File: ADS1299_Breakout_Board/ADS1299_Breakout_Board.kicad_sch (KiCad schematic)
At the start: 41 parts, among them J1 Conn_01x08_Pin, J2 Conn_01x08_Pin, J3 Conn_01x08_Pin, J4 Conn_01x08_Pin, J5 Conn_01x08_Pin, U1 TPD4E1B06DRLR, U2 ADS1299IPAG, U3 TPD4E1B06DRLR, U4 TPD4E1B06DRLR, U5 TPD4E1B06DRLR, U6 TPD4E1B06DRLR, U7 TPD4E1B06DRLR

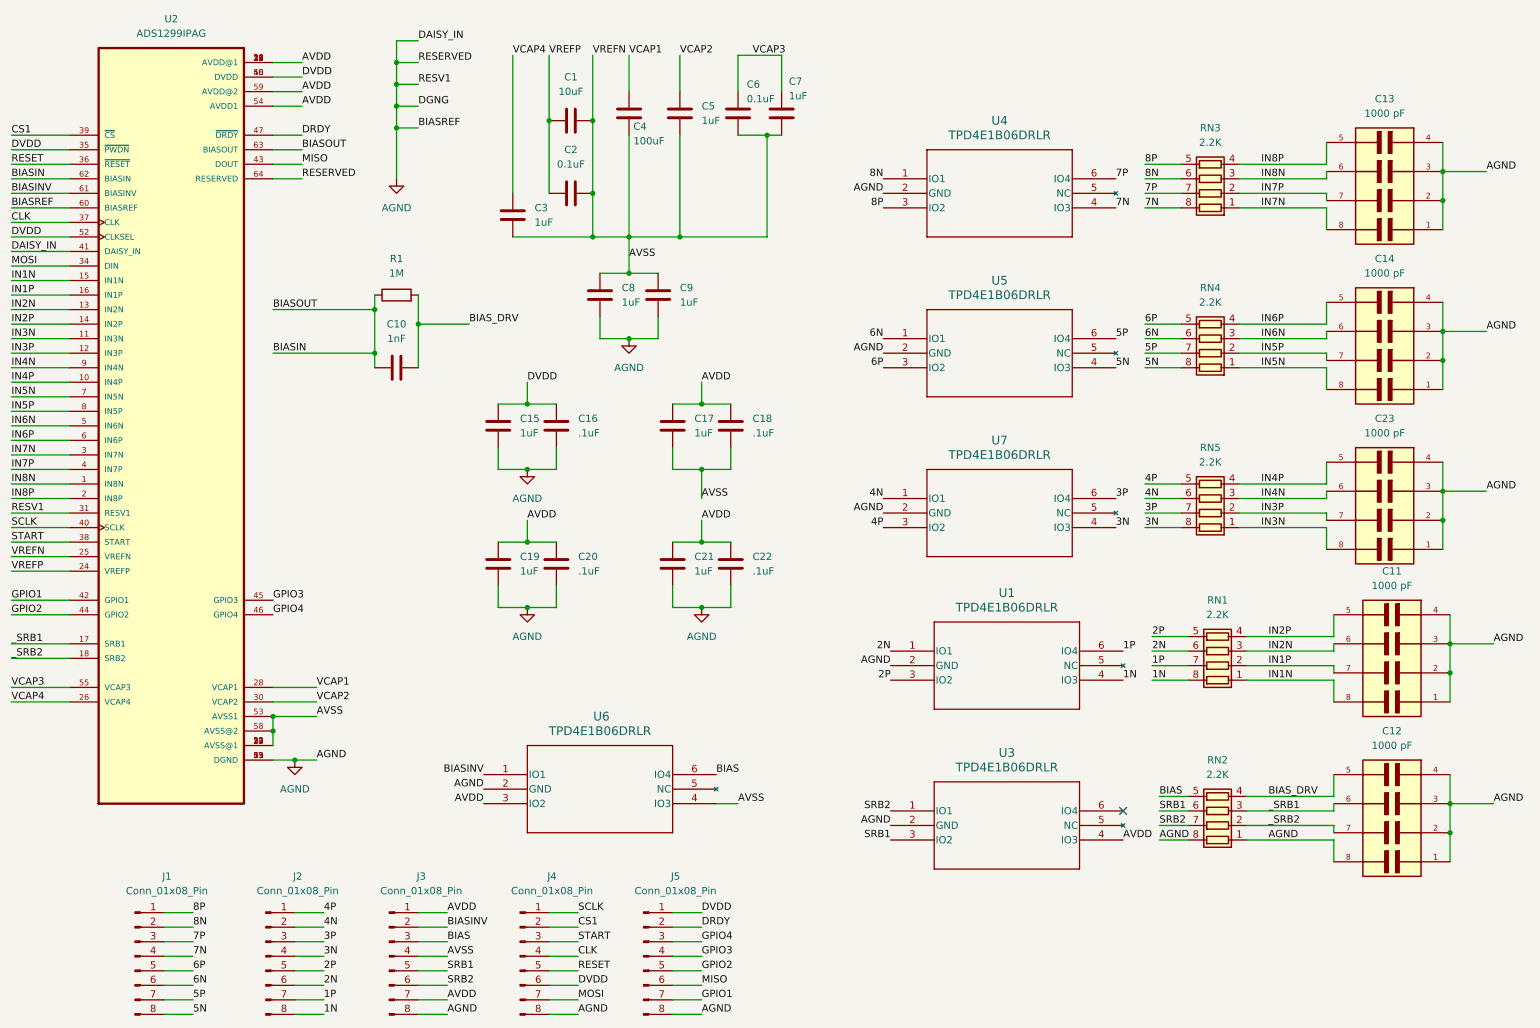
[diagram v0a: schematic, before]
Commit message: Linked Footprint libraries
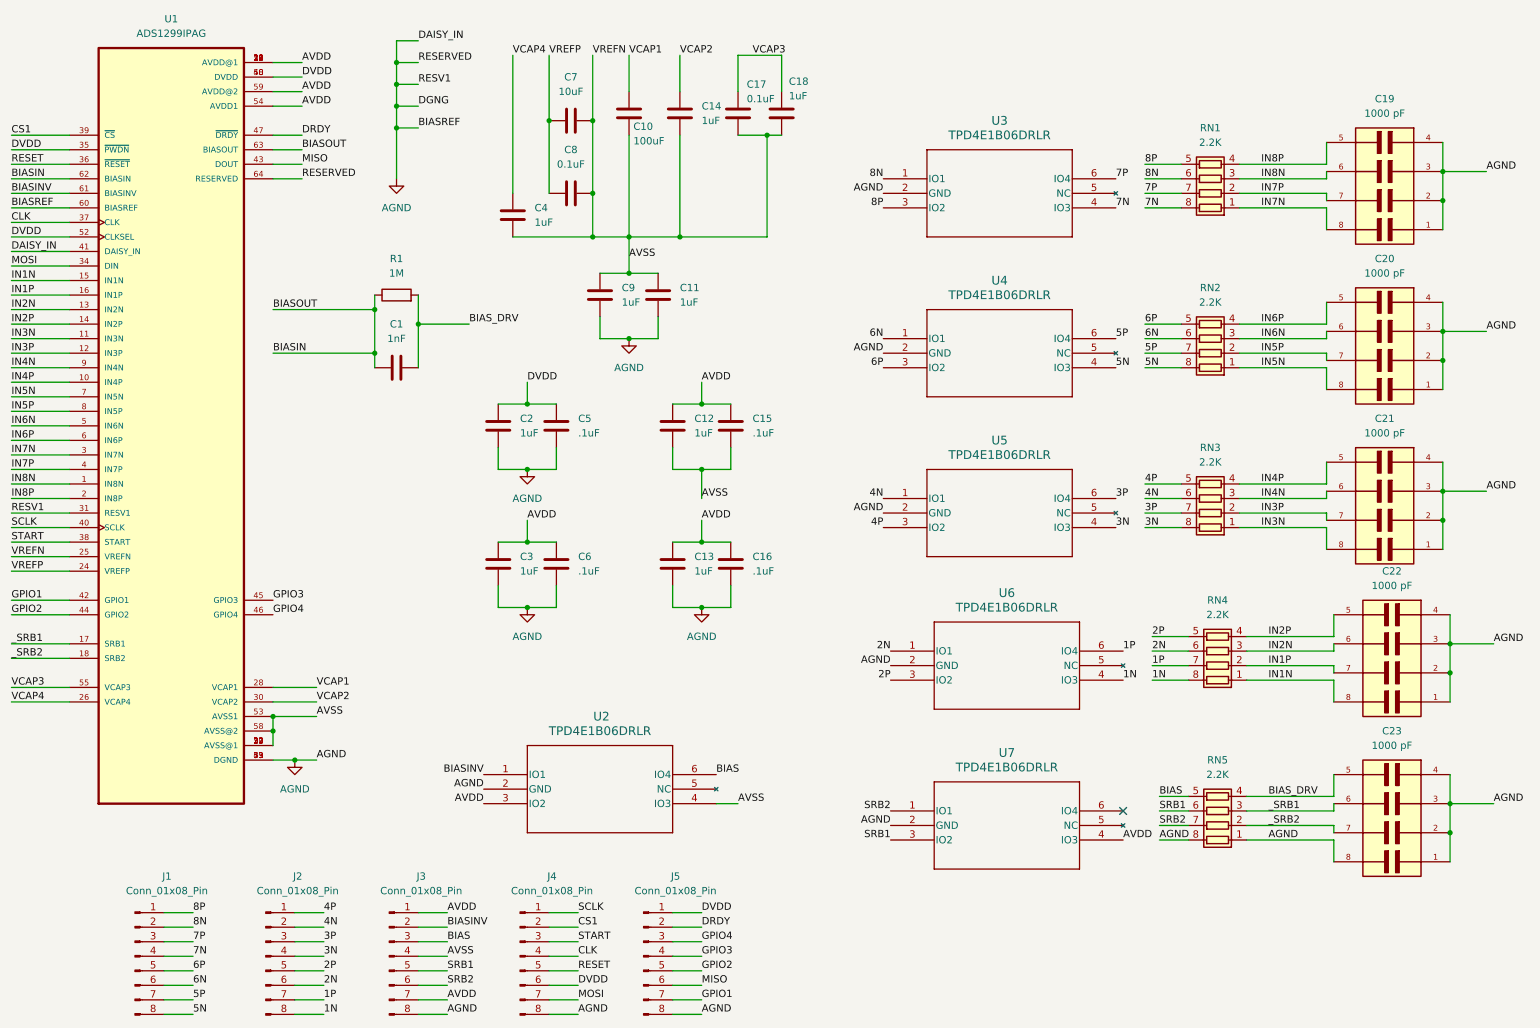
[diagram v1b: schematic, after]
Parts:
- C19: renamed from C13; footprint CAPCAF50P200X125X85-8 -> W3A45C102K4T2A:CAPCAF50P200X125X85-8
- C20: renamed from C14; footprint CAPCAF50P200X125X85-8 -> W3A45C102K4T2A:CAPCAF50P200X125X85-8
- C21: renamed from C23; footprint CAPCAF50P200X125X85-8 -> W3A45C102K4T2A:CAPCAF50P200X125X85-8
- C22: renamed from C11; footprint CAPCAF50P200X125X85-8 -> W3A45C102K4T2A:CAPCAF50P200X125X85-8
- C23: renamed from C12; footprint CAPCAF50P200X125X85-8 -> W3A45C102K4T2A:CAPCAF50P200X125X85-8
- U1: renamed from U2; footprint QFP50P1200X1200X120-64N -> ADS1299:QFP50P1200X1200X120-64N
- U2: renamed from U6; footprint DRL6_TEX -> TPD4E1B06:DRL6_TEX
- U3: renamed from U4; footprint DRL6_TEX -> TPD4E1B06:DRL6_TEX
- U4: renamed from U5; footprint DRL6_TEX -> TPD4E1B06:DRL6_TEX
- U5: renamed from U7; footprint DRL6_TEX -> TPD4E1B06:DRL6_TEX
- U6: renamed from U1; footprint DRL6_TEX -> TPD4E1B06:DRL6_TEX
- U7: renamed from U3; footprint DRL6_TEX -> TPD4E1B06:DRL6_TEX
- renumbered C10 to C1, C4 to C10, C9 to C11, C17 to C12, C21 to C13, C5 to C14, C18 to C15, C22 to C16, C6 to C17, C7 to C18, C15 to C2, C19 to C3, C3 to C4, C16 to C5, C20 to C6, C1 to C7, C2 to C8, C8 to C9, RN3 to RN1, RN4 to RN2, RN5 to RN3, RN1 to RN4, RN2 to RN5
